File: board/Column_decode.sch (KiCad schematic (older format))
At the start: 6 parts, among them U15 74HC238BQ, U16 74HC238BQ, U17 74HC238BQ

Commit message: Updated the footprints in the schematic having renamed all of my published libraries
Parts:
- C29, C30, C31: footprint rcl:C0603 -> rhais_rcl:C0603
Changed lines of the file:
@@
 $Descr A4 11693 8268
 encoding utf-8
-Sheet 5 6
+Sheet 4 6
 Title ""
 Date ""
@@
 F 0 "C30" V 7200 2900 59  0000 C CNN
 F 1 "0.1uF" V 7400 2900 59  0000 C CNN
-F 2 "rcl:C0603" H 7300 2900 50  0001 C CNN
+F 2 "rhais_rcl:C0603" H 7300 2900 50  0001 C CNN
 F 3 "" H 7300 2900 50  0001 C CNN
 F 4 "Multicomp" H 7300 2900 59  0001 L BNN "MFR"
@@
 F 0 "C31" V 9600 2900 59  0000 C CNN
 F 1 "0.1uF" V 9800 2900 59  0000 C CNN
-F 2 "rcl:C0603" H 9700 2900 50  0001 C CNN
+F 2 "rhais_rcl:C0603" H 9700 2900 50  0001 C CNN
 F 3 "" H 9700 2900 50  0001 C CNN
 F 4 "Multicomp" H 9700 2900 59  0001 L BNN "MFR"
@@
 F 0 "C29" V 4800 2900 59  0000 C CNN
 F 1 "0.1uF" V 5000 2900 59  0000 C CNN
-F 2 "rcl:C0603" H 4900 2900 50  0001 C CNN
+F 2 "rhais_rcl:C0603" H 4900 2900 50  0001 C CNN
 F 3 "" H 4900 2900 50  0001 C CNN
 F 4 "Multicomp" H 4900 2900 59  0001 L BNN "MFR"

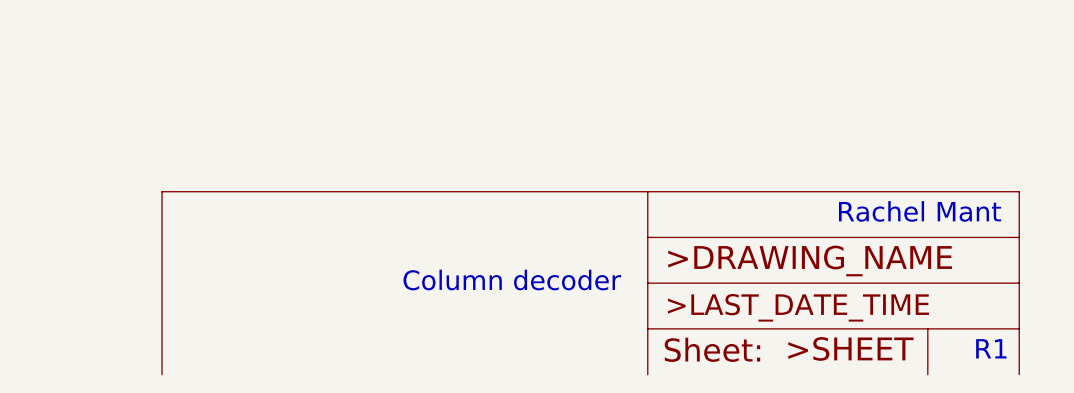
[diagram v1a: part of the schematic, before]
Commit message: Fixed up the schematics metadata to properly capture revision, block and authorship information
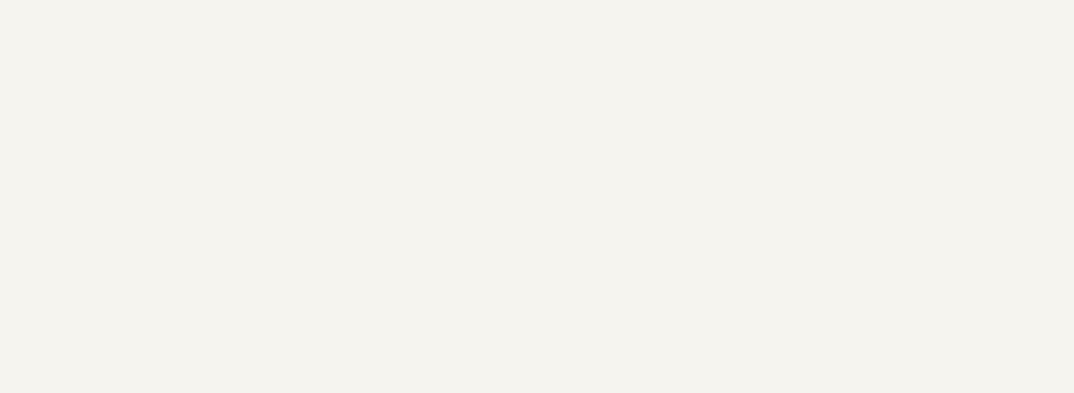
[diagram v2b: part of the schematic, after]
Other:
- note removed: "Column decoder"
- note removed: "R1"
- note removed: "Rachel Mant"
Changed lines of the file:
@@
 encoding utf-8
 Sheet 4 6
-Title ""
+Title "Column decoder"
 Date ""
-Rev ""
-Comp ""
+Rev "1"
+Comp "Rachel Mant"
 Comment1 ""
 Comment2 ""
@@
 	1    0    0    -1
 $EndComp
-$Comp
-L MXKeyboard_RGB-eagle-import:A4L-LOC #FRAME2
-U 1 1 DFE0E5A0
-P 900 6400
-AR Path="/DFE0E5A0" Ref="#FRAME2"  Part="1"
-AR Path="/5F5D661B/DFE0E5A0" Ref="#FRAME2"  Part="1"
-F 0 "#FRAME2" H 900 6400 50  0001 C CNN
-F 1 "A4L-LOC" H 900 6400 50  0001 C CNN
-F 2 "" H 900 6400 50  0001 C CNN
-F 3 "" H 900 6400 50  0001 C CNN
-	1    900  6400
-	1    0    0    -1
-$EndComp
 Text Notes 2700 2200 0    59   ~ 0
 Active when DCOL[5..4] == 00
@@
 Text Notes 7500 2200 0    59   ~ 0
 Active when DCOL[5..4] == 10
-Text Notes 8300 5900 0    85   ~ 0
-Column decoder
-Text Notes 10200 5600 0    85   ~ 0
-Rachel Mant
-Text Notes 10800 6200 0    85   ~ 0
-R1
 $Comp
 L power:GND #PWR053

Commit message: Switched the 3-to-8 decoders to use my DHVQFN-16 part from rhais_package-qfn
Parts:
- U15, U16, U17: footprint MXKeyboard_RGB:DHVQFN-16 -> rhais_package-qfn:DQFN16_1EP_2.5x3.5mm_P0.5mm
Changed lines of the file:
@@
 	7550 3700 7650 3800
-$Comp
-L MXKeyboard_RGB-eagle-import:74HC238BQ U15
-U 1 1 6D3D1EC3
-P 3700 3100
-AR Path="/6D3D1EC3" Ref="U15"  Part="1"
-AR Path="/5F5D661B/6D3D1EC3" Ref="U15"  Part="1"
-F 0 "U15" H 3700 3100 50  0001 C CNN
-F 1 "74HC238BQ" H 3700 3100 50  0001 C CNN
-F 2 "MXKeyboard_RGB:DHVQFN-16" H 3700 3100 50  0001 C CNN
-F 3 "" H 3700 3100 50  0001 C CNN
-	1    3700 3100
-	1    0    0    -1
-$EndComp
-$Comp
-L MXKeyboard_RGB-eagle-import:74HC238BQ U16
-U 1 1 3D1E7172
-P 6100 3100
-AR Path="/3D1E7172" Ref="U16"  Part="1"
-AR Path="/5F5D661B/3D1E7172" Ref="U16"  Part="1"
-F 0 "U16" H 6100 3100 50  0001 C CNN
-F 1 "74HC238BQ" H 6100 3100 50  0001 C CNN
-F 2 "MXKeyboard_RGB:DHVQFN-16" H 6100 3100 50  0001 C CNN
-F 3 "" H 6100 3100 50  0001 C CNN
-	1    6100 3100
-	1    0    0    -1
-$EndComp
 $Comp
 L Device:C_Small C30
@@
 F 3 "" H 8900 3800 50  0001 C CNN
 	1    8900 3800
-	1    0    0    -1
-$EndComp
-$Comp
-L MXKeyboard_RGB-eagle-import:74HC238BQ U17
-U 1 1 E1651699
-P 8500 3100
-AR Path="/E1651699" Ref="U17"  Part="1"
-AR Path="/5F5D661B/E1651699" Ref="U17"  Part="1"
-F 0 "U17" H 8500 3100 50  0001 C CNN
-F 1 "74HC238BQ" H 8500 3100 50  0001 C CNN
-F 2 "MXKeyboard_RGB:DHVQFN-16" H 8500 3100 50  0001 C CNN
-F 3 "" H 8500 3100 50  0001 C CNN
-	1    8500 3100
 	1    0    0    -1
 $EndComp
@@
 NoConn ~ 9300 3100
 NoConn ~ 9300 3200
+$Comp
+L MXKeyboard_RGB-eagle-import:74HC238BQ U17
+U 1 1 E1651699
+P 8500 3100
+AR Path="/E1651699" Ref="U17"  Part="1"
+AR Path="/5F5D661B/E1651699" Ref="U17"  Part="1"
+F 0 "U17" H 8500 3100 50  0001 C CNN
+F 1 "74HC238BQ" H 8500 3100 50  0001 C CNN
+F 2 "rhais_package-qfn:DQFN16_1EP_2.5x3.5mm_P0.5mm" H 8500 3100 50  0001 C CNN
+F 3 "" H 8500 3100 50  0001 C CNN
+	1    8500 3100
+	1    0    0    -1
+$EndComp
+$Comp
+L MXKeyboard_RGB-eagle-import:74HC238BQ U16
+U 1 1 3D1E7172
+P 6100 3100
+AR Path="/3D1E7172" Ref="U16"  Part="1"
+AR Path="/5F5D661B/3D1E7172" Ref="U16"  Part="1"
+F 0 "U16" H 6100 3100 50  0001 C CNN
+F 1 "74HC238BQ" H 6100 3100 50  0001 C CNN
+F 2 "rhais_package-qfn:DQFN16_1EP_2.5x3.5mm_P0.5mm" H 6100 3100 50  0001 C CNN
+F 3 "" H 6100 3100 50  0001 C CNN
+	1    6100 3100
+	1    0    0    -1
+$EndComp
+$Comp
+L MXKeyboard_RGB-eagle-import:74HC238BQ U15
+U 1 1 6D3D1EC3
+P 3700 3100
+AR Path="/6D3D1EC3" Ref="U15"  Part="1"
+AR Path="/5F5D661B/6D3D1EC3" Ref="U15"  Part="1"
+F 0 "U15" H 3700 3100 50  0001 C CNN
+F 1 "74HC238BQ" H 3700 3100 50  0001 C CNN
+F 2 "rhais_package-qfn:DQFN16_1EP_2.5x3.5mm_P0.5mm" H 3700 3100 50  0001 C CNN
+F 3 "" H 3700 3100 50  0001 C CNN
+	1    3700 3100
+	1    0    0    -1
+$EndComp
 Wire Bus Line
 	7550 2500 7550 3700

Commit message: Renamed MXKeyboard_RGB => MXKeyboard and cleaned up the last of the old Eagle files we aren't using now
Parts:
- U15, U16, U17: symbol MXKeyboard_RGB-eagle-import:74HC238BQ -> MXKeyboard-eagle-import:74HC238BQ
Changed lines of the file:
@@
 NoConn ~ 9300 3200
 $Comp
-L MXKeyboard_RGB-eagle-import:74HC238BQ U17
+L MXKeyboard-eagle-import:74HC238BQ U17
 U 1 1 E1651699
 P 8500 3100
@@
 $EndComp
 $Comp
-L MXKeyboard_RGB-eagle-import:74HC238BQ U16
+L MXKeyboard-eagle-import:74HC238BQ U16
 U 1 1 3D1E7172
 P 6100 3100
@@
 $EndComp
 $Comp
-L MXKeyboard_RGB-eagle-import:74HC238BQ U15
+L MXKeyboard-eagle-import:74HC238BQ U15
 U 1 1 6D3D1EC3
 P 3700 3100

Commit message: Cleaned up the BOM and added all the missing BOM information I could find
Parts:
- C29, C30, C31: URL_FARNELL (none) -> https://uk.farnell.com/multicomp/mc0603b104j250ct/cap-0-1-f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
- U15, U16, U17: MFR (none) -> Nexperia; MPN (none) -> 74HC238BQ,115; OC_FARNELL (none) -> 2164750; URL_FARNELL (none) -> https://uk.farnell.com/nexperia/74hc238bq/ic-3-8-line-decod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
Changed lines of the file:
@@
 F 1 "0.1uF" V 7400 2900 59  0000 C CNN
 F 2 "rhais_rcl:C0603" H 7300 2900 50  0001 C CNN
-F 3 "" H 7300 2900 50  0001 C CNN
+F 3 "http://www.farnell.com/datasheets/1870456.pdf" H 7300 2900 50  0001 C CNN
 F 4 "Multicomp" H 7300 2900 59  0001 L BNN "MFR"
 F 5 "MC0603B104J250CT" H 7300 2900 59  0001 L BNN "MPN"
 F 6 "2310559" H 7300 2900 59  0001 L BNN "OC_FARNELL"
+F 7 "https://uk.farnell.com/multicomp/mc0603b104j250ct/cap-0-1-f-25v-5-x7r-0603-reel/dp/2310559" H 7300 2900 50  0001 C CNN "URL_FARNELL"
 	1    7300 2900
 	1    0    0    -1
@@
 F 1 "0.1uF" V 9800 2900 59  0000 C CNN
 F 2 "rhais_rcl:C0603" H 9700 2900 50  0001 C CNN
-F 3 "" H 9700 2900 50  0001 C CNN
+F 3 "http://www.farnell.com/datasheets/1870456.pdf" H 9700 2900 50  0001 C CNN
 F 4 "Multicomp" H 9700 2900 59  0001 L BNN "MFR"
 F 5 "MC0603B104J250CT" H 9700 2900 59  0001 L BNN "MPN"
 F 6 "2310559" H 9700 2900 59  0001 L BNN "OC_FARNELL"
+F 7 "https://uk.farnell.com/multicomp/mc0603b104j250ct/cap-0-1-f-25v-5-x7r-0603-reel/dp/2310559" H 9700 2900 50  0001 C CNN "URL_FARNELL"
 	1    9700 2900
 	1    0    0    -1
@@
 F 1 "0.1uF" V 5000 2900 59  0000 C CNN
 F 2 "rhais_rcl:C0603" H 4900 2900 50  0001 C CNN
-F 3 "" H 4900 2900 50  0001 C CNN
+F 3 "http://www.farnell.com/datasheets/1870456.pdf" H 4900 2900 50  0001 C CNN
 F 4 "Multicomp" H 4900 2900 59  0001 L BNN "MFR"
 F 5 "MC0603B104J250CT" H 4900 2900 59  0001 L BNN "MPN"
 F 6 "2310559" H 4900 2900 59  0001 L BNN "OC_FARNELL"
+F 7 "https://uk.farnell.com/multicomp/mc0603b104j250ct/cap-0-1-f-25v-5-x7r-0603-reel/dp/2310559" H 4900 2900 50  0001 C CNN "URL_FARNELL"
 	1    4900 2900
 	1    0    0    -1
@@
 F 1 "74HC238BQ" H 8500 3100 50  0001 C CNN
 F 2 "rhais_package-qfn:DQFN16_1EP_2.5x3.5mm_P0.5mm" H 8500 3100 50  0001 C CNN
-F 3 "" H 8500 3100 50  0001 C CNN
+F 3 "https://assets.nexperia.com/documents/data-sheet/74HC_HCT238.pdf" H 8500 3100 50  0001 C CNN
+F 4 "Nexperia" H 8500 3100 50  0001 C CNN "MFR"
+F 5 "74HC238BQ,115" H 8500 3100 50  0001 C CNN "MPN"
+F 6 "2164750" H 8500 3100 50  0001 C CNN "OC_FARNELL"
+F 7 "https://uk.farnell.com/nexperia/74hc238bq/ic-3-8-line-decoder-demux-dhvqfn16/dp/2164750" H 8500 3100 50  0001 C CNN "URL_FARNELL"
 	1    8500 3100
 	1    0    0    -1
@@
 F 1 "74HC238BQ" H 6100 3100 50  0001 C CNN
 F 2 "rhais_package-qfn:DQFN16_1EP_2.5x3.5mm_P0.5mm" H 6100 3100 50  0001 C CNN
-F 3 "" H 6100 3100 50  0001 C CNN
+F 3 "https://assets.nexperia.com/documents/data-sheet/74HC_HCT238.pdf" H 6100 3100 50  0001 C CNN
+F 4 "Nexperia" H 6100 3100 50  0001 C CNN "MFR"
+F 5 "74HC238BQ,115" H 6100 3100 50  0001 C CNN "MPN"
+F 6 "2164750" H 6100 3100 50  0001 C CNN "OC_FARNELL"
+F 7 "https://uk.farnell.com/nexperia/74hc238bq/ic-3-8-line-decoder-demux-dhvqfn16/dp/2164750" H 6100 3100 50  0001 C CNN "URL_FARNELL"
 	1    6100 3100
 	1    0    0    -1
@@
 F 1 "74HC238BQ" H 3700 3100 50  0001 C CNN
 F 2 "rhais_package-qfn:DQFN16_1EP_2.5x3.5mm_P0.5mm" H 3700 3100 50  0001 C CNN
-F 3 "" H 3700 3100 50  0001 C CNN
+F 3 "https://assets.nexperia.com/documents/data-sheet/74HC_HCT238.pdf" H 3700 3100 50  0001 C CNN
+F 4 "Nexperia" H 3700 3100 50  0001 C CNN "MFR"
+F 5 "74HC238BQ,115" H 3700 3100 50  0001 C CNN "MPN"
+F 6 "2164750" H 3700 3100 50  0001 C CNN "OC_FARNELL"
+F 7 "https://uk.farnell.com/nexperia/74hc238bq/ic-3-8-line-decoder-demux-dhvqfn16/dp/2164750" H 3700 3100 50  0001 C CNN "URL_FARNELL"
 	1    3700 3100
 	1    0    0    -1
